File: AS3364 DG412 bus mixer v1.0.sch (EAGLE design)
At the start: 119 parts, among them IC1 PCA9539PW, IC10 DG412-J, IC11 DG412-J, IC14 TL074JT, IC2 TL074JT, IC3 TL072JT, IC4 TL074JT, IC6 TL072JT, IC8 DG412-J, IC9 DG412-J

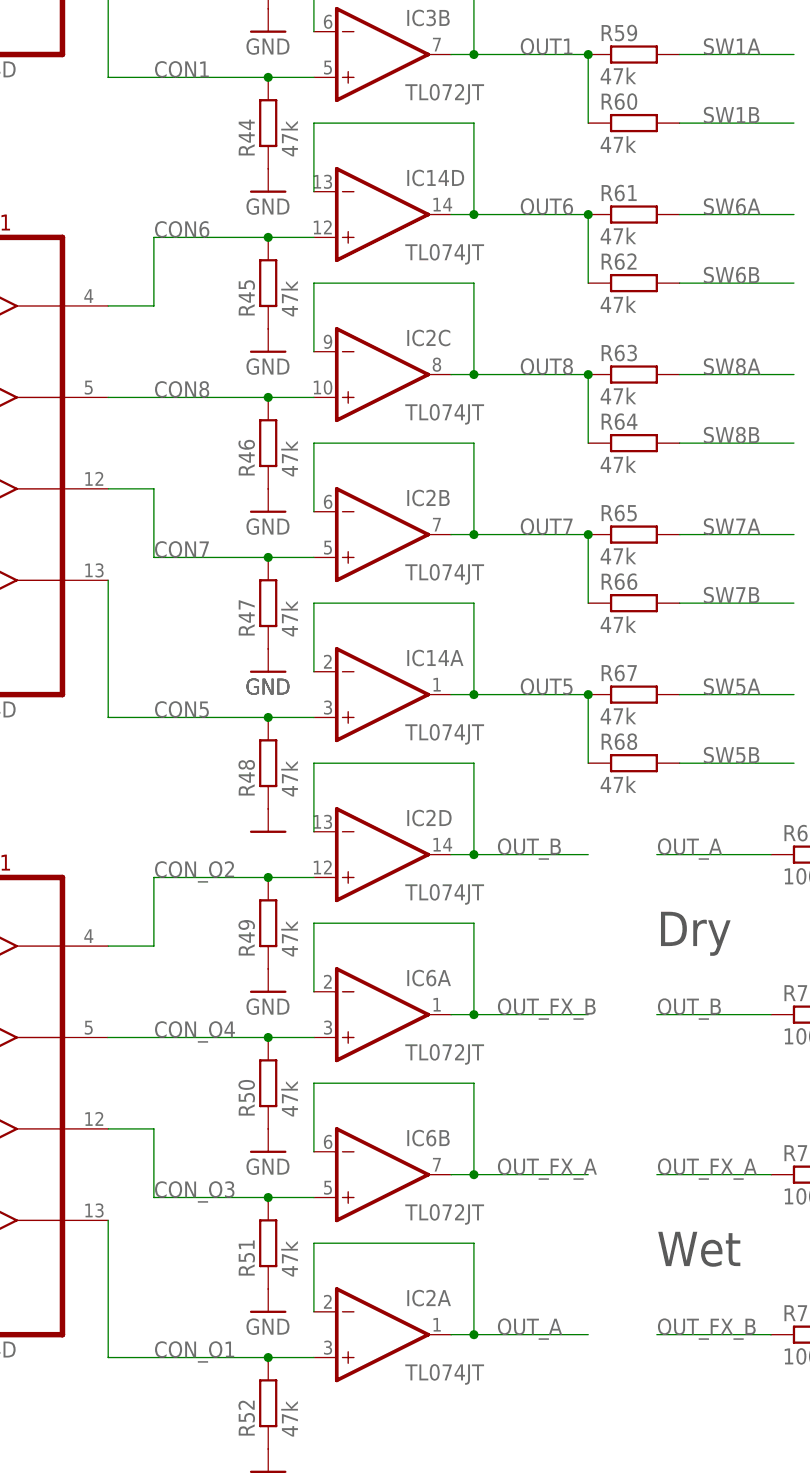
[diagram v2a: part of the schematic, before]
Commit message: Moved dry/wet bus mixer to center to shorten vca-switch distances
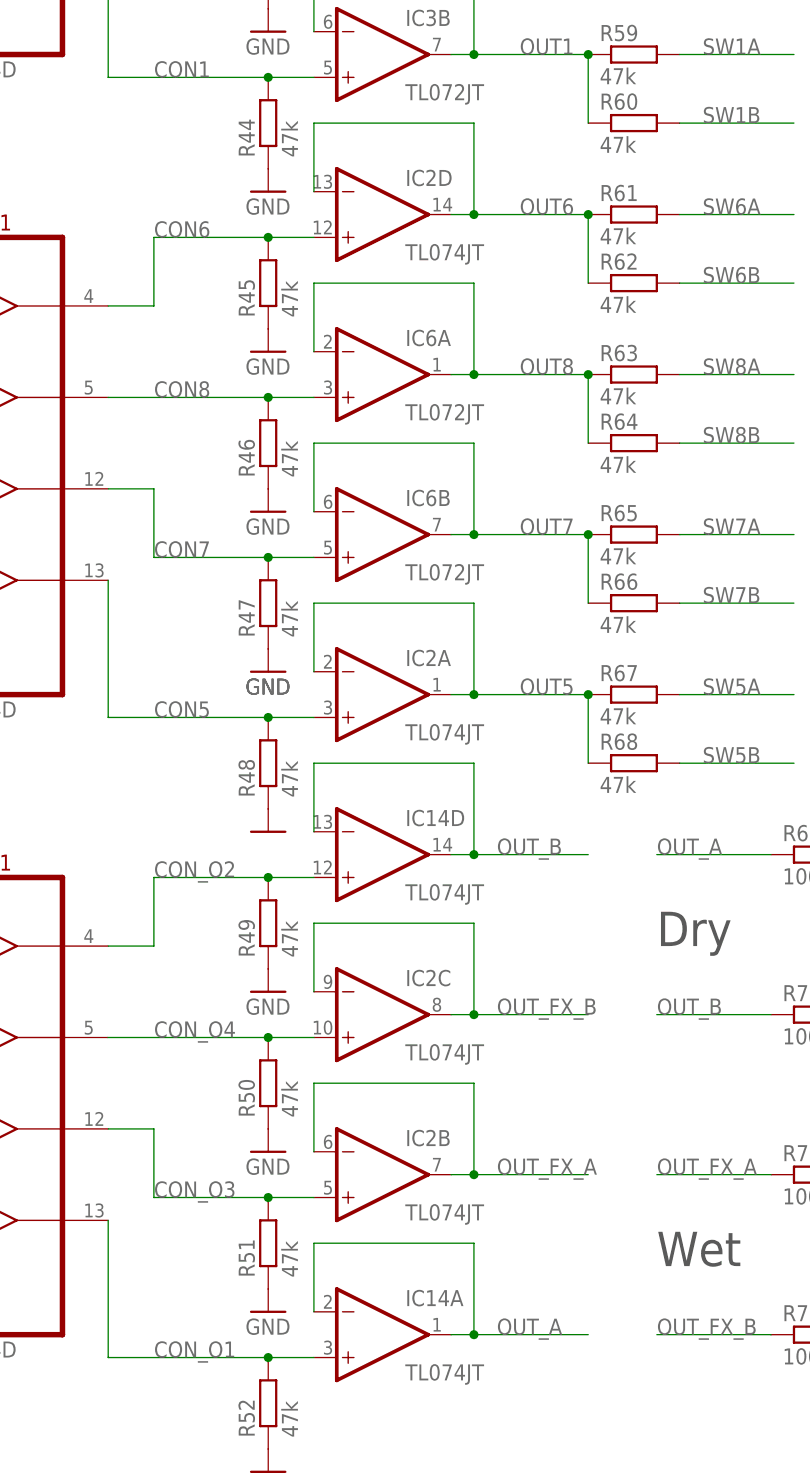
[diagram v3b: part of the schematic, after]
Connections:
- net CON5: now also IC2A.+IN; no longer IC14A.+IN
- net CON6: now also IC2D.+IN; no longer IC14D.+IN
- net CON7: now also IC6B.+IN; no longer IC2B.+IN
- net CON8: now also IC6A.+IN; no longer IC2C.+IN
- net CON_O1: now also IC14A.+IN; no longer IC2A.+IN
- net CON_O2: now also IC14D.+IN; no longer IC2D.+IN
- net CON_O3: now also IC2B.+IN; no longer IC6B.+IN
- net CON_O4: now also IC2C.+IN; no longer IC6A.+IN
- net OUT5: now also IC2A.-IN, IC2A.OUT; no longer IC14A.-IN, IC14A.OUT
- net OUT6: now also IC2D.-IN, IC2D.OUT; no longer IC14D.-IN, IC14D.OUT
- net OUT7: now also IC6B.-IN, IC6B.OUT; no longer IC2B.-IN, IC2B.OUT
- net OUT8: now also IC6A.-IN, IC6A.OUT; no longer IC2C.-IN, IC2C.OUT
- net OUT_A: now also IC14A.-IN, IC14A.OUT; no longer IC2A.-IN, IC2A.OUT
- net OUT_B: now also IC14D.-IN, IC14D.OUT; no longer IC2D.-IN, IC2D.OUT
- net OUT_FX_A: now also IC2B.-IN, IC2B.OUT; no longer IC6B.-IN, IC6B.OUT
- net OUT_FX_B: now also IC2C.-IN, IC2C.OUT; no longer IC6A.-IN, IC6A.OUT
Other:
- moved on the sheet: IC14A, IC14D, IC2A, IC2B, IC2C, IC2D, IC6A, IC6B
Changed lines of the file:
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@@
 <attribute name="VALUE" x="-27.94" y="-71.12" size="1.778" layer="96"/>
-</instance>
-<instance part="IC6" gate="B" x="73.66" y="-93.98" smashed="yes">
-<attribute name="NAME" x="76.2" y="-90.805" size="1.778" layer="95"/>
-<attribute name="VALUE" x="76.2" y="-99.06" size="1.778" layer="96"/>
-</instance>
-<instance part="IC6" gate="A" x="73.66" y="-76.2" smashed="yes">
-<attribute name="NAME" x="76.2" y="-73.025" size="1.778" layer="95"/>
-<attribute name="VALUE" x="76.2" y="-81.28" size="1.778" layer="96"/>
 </instance>
 <instance part="C15" gate="G$1" x="-7.62" y="-109.22" smashed="yes" rot="R90">
@@
 </instance>
 <instance part="IC4" gate="P" x="149.86" y="-167.64" smashed="yes"/>
-<instance part="IC14" gate="A" x="73.66" y="-40.64" smashed="yes">
-<attribute name="NAME" x="76.2" y="-37.465" size="1.778" layer="95"/>
-<attribute name="VALUE" x="76.2" y="-45.72" size="1.778" layer="96"/>
-</instance>
 <instance part="IC14" gate="C" x="73.66" y="66.04" smashed="yes">
 <attribute name="NAME" x="76.2" y="69.215" size="1.778" layer="95"/>
@@
 <attribute name="VALUE" x="76.2" y="43.18" size="1.778" layer="96"/>
 </instance>
-<instance part="IC14" gate="D" x="73.66" y="12.7" smashed="yes">
-<attribute name="NAME" x="76.2" y="15.875" size="1.778" layer="95"/>
-<attribute name="VALUE" x="76.2" y="7.62" size="1.778" layer="96"/>
-</instance>
-<instance part="IC2" gate="C" x="73.66" y="-5.08" smashed="yes">
-<attribute name="NAME" x="76.2" y="-1.905" size="1.778" layer="95"/>
-<attribute name="VALUE" x="76.2" y="-10.16" size="1.778" layer="96"/>
-</instance>
-<instance part="IC2" gate="A" x="73.66" y="-111.76" smashed="yes">
-<attribute name="NAME" x="76.2" y="-108.585" size="1.778" layer="95"/>
-<attribute name="VALUE" x="76.2" y="-116.84" size="1.778" layer="96"/>
-</instance>
-<instance part="IC2" gate="B" x="73.66" y="-22.86" smashed="yes">
-<attribute name="NAME" x="76.2" y="-19.685" size="1.778" layer="95"/>
-<attribute name="VALUE" x="76.2" y="-27.94" size="1.778" layer="96"/>
-</instance>
-<instance part="IC2" gate="D" x="73.66" y="-58.42" smashed="yes">
-<attribute name="NAME" x="76.2" y="-55.245" size="1.778" layer="95"/>
-<attribute name="VALUE" x="76.2" y="-63.5" size="1.778" layer="96"/>
-</instance>
 <instance part="C23" gate="G$1" x="-182.88" y="-33.02" smashed="yes" rot="R180">
 <attribute name="NAME" x="-186.944" y="-28.321" size="1.778" layer="95" rot="R180"/>
 <attribute name="VALUE" x="-186.944" y="-30.861" size="1.778" layer="96" rot="R180"/>
+</instance>
+<instance part="IC2" gate="D" x="73.66" y="12.7" smashed="yes">
+<attribute name="NAME" x="76.2" y="15.875" size="1.778" layer="95"/>
+<attribute name="VALUE" x="76.2" y="7.62" size="1.778" layer="96"/>
+</instance>
+<instance part="IC14" gate="D" x="73.66" y="-58.42" smashed="yes">
+<attribute name="NAME" x="76.2" y="-55.245" size="1.778" layer="95"/>
+<attribute name="VALUE" x="76.2" y="-63.5" size="1.778" layer="96"/>
+</instance>
+<instance part="IC2" gate="A" x="73.66" y="-40.64" smashed="yes">
+<attribute name="NAME" x="76.2" y="-37.465" size="1.778" layer="95"/>
+<attribute name="VALUE" x="76.2" y="-45.72" size="1.778" layer="96"/>
+</instance>
+<instance part="IC14" gate="A" x="73.66" y="-111.76" smashed="yes">
+<attribute name="NAME" x="76.2" y="-108.585" size="1.778" layer="95"/>
+<attribute name="VALUE" x="76.2" y="-116.84" size="1.778" layer="96"/>
+</instance>
+<instance part="IC2" gate="C" x="73.66" y="-76.2" smashed="yes">
+<attribute name="NAME" x="76.2" y="-73.025" size="1.778" layer="95"/>
+<attribute name="VALUE" x="76.2" y="-81.28" size="1.778" layer="96"/>
+</instance>
+<instance part="IC6" gate="A" x="73.66" y="-5.08" smashed="yes">
+<attribute name="NAME" x="76.2" y="-1.905" size="1.778" layer="95"/>
+<attribute name="VALUE" x="76.2" y="-10.16" size="1.778" layer="96"/>
+</instance>
+<instance part="IC2" gate="B" x="73.66" y="-93.98" smashed="yes">
+<attribute name="NAME" x="76.2" y="-90.805" size="1.778" layer="95"/>
+<attribute name="VALUE" x="76.2" y="-99.06" size="1.778" layer="96"/>
+</instance>
+<instance part="IC6" gate="B" x="73.66" y="-22.86" smashed="yes">
+<attribute name="NAME" x="76.2" y="-19.685" size="1.778" layer="95"/>
+<attribute name="VALUE" x="76.2" y="-27.94" size="1.778" layer="96"/>
 </instance>
 </instances>
@@
 <wire x1="66.04" y1="10.16" x2="60.96" y2="10.16" width="0.1524" layer="91"/>
 <junction x="60.96" y="10.16"/>
-<pinref part="IC14" gate="D" pin="+IN"/>
+<pinref part="IC2" gate="D" pin="+IN"/>
 </segment>
 </net>
@@
 <wire x1="66.04" y1="-7.62" x2="60.96" y2="-7.62" width="0.1524" layer="91"/>
 <junction x="60.96" y="-7.62"/>
-<pinref part="IC2" gate="C" pin="+IN"/>
+<pinref part="IC6" gate="A" pin="+IN"/>
 </segment>
 </net>
@@
 <wire x1="66.04" y1="-25.4" x2="60.96" y2="-25.4" width="0.1524" layer="91"/>
 <junction x="60.96" y="-25.4"/>
-<pinref part="IC2" gate="B" pin="+IN"/>
+<pinref part="IC6" gate="B" pin="+IN"/>
 </segment>
 </net>
@@
 <wire x1="66.04" y1="-43.18" x2="60.96" y2="-43.18" width="0.1524" layer="91"/>
 <junction x="60.96" y="-43.18"/>
-<pinref part="IC14" gate="A" pin="+IN"/>
+<pinref part="IC2" gate="A" pin="+IN"/>
 </segment>
 </net>
@@
 <wire x1="96.52" y1="-22.86" x2="96.52" y2="-30.48" width="0.1524" layer="91"/>
 <junction x="96.52" y="-22.86"/>
-<pinref part="IC2" gate="B" pin="-IN"/>
-<pinref part="IC2" gate="B" pin="OUT"/>
+<pinref part="IC6" gate="B" pin="-IN"/>
+<pinref part="IC6" gate="B" pin="OUT"/>
 </segment>
 </net>
@@
 <wire x1="96.52" y1="-5.08" x2="96.52" y2="-12.7" width="0.1524" layer="91"/>
 <junction x="96.52" y="-5.08"/>
-<pinref part="IC2" gate="C" pin="-IN"/>
-<pinref part="IC2" gate="C" pin="OUT"/>
+<pinref part="IC6" gate="A" pin="-IN"/>
+<pinref part="IC6" gate="A" pin="OUT"/>
 </segment>
 </net>
@@
 <wire x1="96.52" y1="-40.64" x2="96.52" y2="-48.26" width="0.1524" layer="91"/>
 <junction x="96.52" y="-40.64"/>
-<pinref part="IC14" gate="A" pin="-IN"/>
-<pinref part="IC14" gate="A" pin="OUT"/>
+<pinref part="IC2" gate="A" pin="-IN"/>
+<pinref part="IC2" gate="A" pin="OUT"/>
 </segment>
 </net>
@@
 <wire x1="96.52" y1="12.7" x2="96.52" y2="5.08" width="0.1524" layer="91"/>
 <junction x="96.52" y="12.7"/>
-<pinref part="IC14" gate="D" pin="-IN"/>
-<pinref part="IC14" gate="D" pin="OUT"/>
+<pinref part="IC2" gate="D" pin="-IN"/>
+<pinref part="IC2" gate="D" pin="OUT"/>
 </segment>
 </net>
@@
 <wire x1="66.04" y1="-60.96" x2="60.96" y2="-60.96" width="0.1524" layer="91"/>
 <junction x="60.96" y="-60.96"/>
-<pinref part="IC2" gate="D" pin="+IN"/>
+<pinref part="IC14" gate="D" pin="+IN"/>
 </segment>
 </net>
@@
 <label x="48.26" y="-78.74" size="1.778" layer="95"/>
 <pinref part="R50" gate="G$1" pin="2"/>
-<pinref part="IC6" gate="A" pin="+IN"/>
 <wire x1="60.96" y1="-78.74" x2="66.04" y2="-78.74" width="0.1524" layer="91"/>
 <junction x="60.96" y="-78.74"/>
+<pinref part="IC2" gate="C" pin="+IN"/>
 </segment>
 </net>
@@
 <pinref part="R51" gate="G$1" pin="2"/>
 <wire x1="48.26" y1="-96.52" x2="60.96" y2="-96.52" width="0.1524" layer="91"/>
-<pinref part="IC6" gate="B" pin="+IN"/>
 <wire x1="66.04" y1="-96.52" x2="60.96" y2="-96.52" width="0.1524" layer="91"/>
 <junction x="60.96" y="-96.52"/>
+<pinref part="IC2" gate="B" pin="+IN"/>
 </segment>
 </net>
@@
 <wire x1="66.04" y1="-114.3" x2="60.96" y2="-114.3" width="0.1524" layer="91"/>
 <junction x="60.96" y="-114.3"/>
-<pinref part="IC2" gate="A" pin="+IN"/>
+<pinref part="IC14" gate="A" pin="+IN"/>
 </segment>
 </net>
@@
 <wire x1="83.82" y1="-76.2" x2="96.52" y2="-76.2" width="0.1524" layer="91"/>
 <junction x="83.82" y="-76.2"/>
-<pinref part="IC6" gate="A" pin="OUT"/>
 <wire x1="66.04" y1="-73.66" x2="66.04" y2="-66.04" width="0.1524" layer="91"/>
-<pinref part="IC6" gate="A" pin="-IN"/>
 <wire x1="66.04" y1="-66.04" x2="83.82" y2="-66.04" width="0.1524" layer="91"/>
 <label x="86.36" y="-76.2" size="1.778" layer="95"/>
+<pinref part="IC2" gate="C" pin="-IN"/>
+<pinref part="IC2" gate="C" pin="OUT"/>
 </segment>
 <segment>
@@
 <wire x1="83.82" y1="-93.98" x2="96.52" y2="-93.98" width="0.1524" layer="91"/>
 <junction x="83.82" y="-93.98"/>
-<pinref part="IC6" gate="B" pin="OUT"/>
 <wire x1="66.04" y1="-91.44" x2="66.04" y2="-83.82" width="0.1524" layer="91"/>
-<pinref part="IC6" gate="B" pin="-IN"/>
 <wire x1="83.82" y1="-83.82" x2="66.04" y2="-83.82" width="0.1524" layer="91"/>
 <label x="86.36" y="-93.98" size="1.778" layer="95"/>
+<pinref part="IC2" gate="B" pin="-IN"/>
+<pinref part="IC2" gate="B" pin="OUT"/>
 </segment>
 <segment>
@@
 <wire x1="66.04" y1="-101.6" x2="83.82" y2="-101.6" width="0.1524" layer="91"/>
 <label x="86.36" y="-111.76" size="1.778" layer="95"/>
-<pinref part="IC2" gate="A" pin="-IN"/>
-<pinref part="IC2" gate="A" pin="OUT"/>
+<pinref part="IC14" gate="A" pin="-IN"/>
+<pinref part="IC14" gate="A" pin="OUT"/>
 </segment>
 <segment>
@@
 <wire x1="66.04" y1="-48.26" x2="83.82" y2="-48.26" width="0.1524" layer="91"/>
 <label x="86.36" y="-58.42" size="1.778" layer="95"/>
-<pinref part="IC2" gate="D" pin="-IN"/>
-<pinref part="IC2" gate="D" pin="OUT"/>
-</segment>
-<segment>
+<pinref part="IC14" gate="D" pin="-IN"/>
+<pinref part="IC14" gate="D" pin="OUT"/>
+</segment>
+<segment>

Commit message: Almost all signals routed except outputs
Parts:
- removed SV1: (no value), joakim:MA16-2WJ
- added SV10, SV11, SV12, SV13, SV14, SV15, SV16, SV17, SV18, SV19, SV2, SV20, SV21, SV22, SV23, SV24, SV25, SV26, SV27, SV28, SV29, SV3, SV30, SV31, SV4, SV5, SV6, SV7, SV8, SV9: (no value), joakim:MA01-1JP
- R69, R70, R71, R72: device rcl:R-EU_R0603 -> rcl:R-EU_R0402
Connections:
- new net RST: SV6.1
- net +12V: now also SV21.1; no longer SV1.18
- net +3V3: now also SV2.1; no longer SV1.31
- net -12V: now also SV31.1; no longer SV1.15
- net CV1: now also SV11.1; no longer SV1.26
- net CV2: now also SV12.1; no longer SV1.24
- net CV3: now also SV13.1; no longer SV1.22
- net CV4: now also SV14.1; no longer SV1.20
- net CV5: now also SV27.1; no longer SV1.12
- net CV6: now also SV28.1; no longer SV1.10
- net CV7: now also SV29.1; no longer SV1.8
- net CV8: now also SV30.1; no longer SV1.6
- net CV_A_DRY: now also SV15.1
- net CV_A_WET: now also SV16.1
- net CV_B_DRY: now also SV17.1
- net CV_B_WET: now also SV18.1
- net DGND: now also SV5.1; no longer SV1.29
- net GND: now also SV22.1; no longer SV1.17
- net IN1: now also SV7.1; no longer SV1.25
- net IN2: now also SV8.1; no longer SV1.23
- net IN3: now also SV9.1; no longer SV1.21
- net IN4: now also SV10.1; no longer SV1.19
- net IN5: now also SV23.1; no longer SV1.11
- net IN6: now also SV24.1; no longer SV1.9
- net IN7: now also SV25.1; no longer SV1.7
- net IN8: now also SV26.1; no longer SV1.5
- net LPF_IN_100K_MIX: now also SV20.1
- net SCL: now also SV4.1; no longer SV1.32
- net SDA: now also SV3.1; no longer SV1.30
- net SVF_IN_100K_MIX: now also SV19.1
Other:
- moved on the sheet: C23, IC1, R1

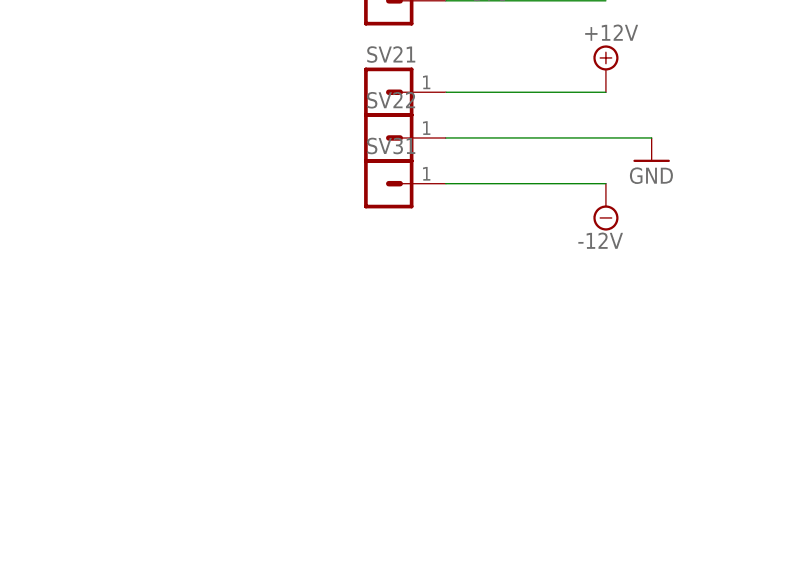
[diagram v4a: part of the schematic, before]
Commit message: Mostly traced, need to do ground and cleanup
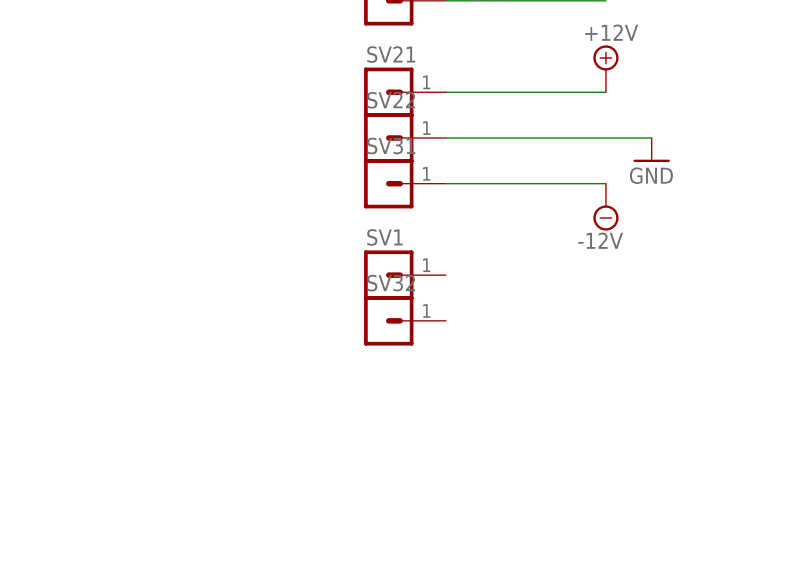
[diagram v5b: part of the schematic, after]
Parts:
- added SV1, SV32: (no value), joakim:MA01-1JP
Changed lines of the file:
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@@
 <part name="SUPPLY3" library="supply2" library_urn="urn:adsk.eagle:library:372" deviceset="+12V" device=""/>
 <part name="SUPPLY4" library="supply2" library_urn="urn:adsk.eagle:library:372" deviceset="-12V" device=""/>
+<part name="SV1" library="joakim" deviceset="MA01-1J" device="P"/>
+<part name="SV32" library="joakim" deviceset="MA01-1J" device="P"/>
 </parts>
 <sheets>
@@
 <attribute name="VALUE" x="-79.375" y="-83.439" size="1.778" layer="96"/>
 </instance>
+<instance part="SV1" gate="G$1" x="-101.6" y="-86.36" smashed="yes">
+<attribute name="VALUE" x="-102.87" y="-91.44" size="1.778" layer="96"/>
+<attribute name="NAME" x="-102.87" y="-83.058" size="1.778" layer="95"/>
+</instance>
+<instance part="SV32" gate="G$1" x="-101.6" y="-91.44" smashed="yes">
+<attribute name="VALUE" x="-102.87" y="-96.52" size="1.778" layer="96"/>
+<attribute name="NAME" x="-102.87" y="-88.138" size="1.778" layer="95"/>
+</instance>
 </instances>

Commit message: Finished tracing, need part numbers
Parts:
- R1: value 1K -> 10k; device rcl:R-EU_R0603 -> rcl:R-EU_R0402
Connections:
- net N$4 renamed VL
- removed net N$81: IC1.!RESET, R1.2
- removed net RST: SV6.1
- new net !RST: IC1.!RESET, R1.2, SV6.1
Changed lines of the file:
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@@
 <part name="+3V17" library="supply1" library_urn="urn:adsk.eagle:library:371" deviceset="+3V3" device=""/>
 <part name="SUPPLY30" library="supply2" library_urn="urn:adsk.eagle:library:372" deviceset="DGND" device=""/>
-<part name="R1" library="rcl" library_urn="urn:adsk.eagle:library:334" deviceset="R-EU_" device="R0603" package3d_urn="urn:adsk.eagle:package:23555/3" value="1K"/>
+<part name="R1" library="rcl" library_urn="urn:adsk.eagle:library:334" deviceset="R-EU_" device="R0402" package3d_urn="urn:adsk.eagle:package:23547/3" value="10k"/>
 <part name="+3V21" library="supply1" library_urn="urn:adsk.eagle:library:371" deviceset="+3V3" device=""/>
 <part name="C10" library="rcl" library_urn="urn:adsk.eagle:library:334" deviceset="C-EU" device="C0402" package3d_urn="urn:adsk.eagle:package:23626/2" value="100nF"/>
@@
 </segment>
 </net>
-<net name="N$81" class="0">
-<segment>
-<pinref part="IC1" gate="G$1" pin="!RESET"/>
-<pinref part="R1" gate="G$1" pin="2"/>
-</segment>
-</net>
-<net name="N$4" class="0">
+<net name="VL" class="0">
 <segment>
 <pinref part="IC8" gate="_WL" pin="VL"/>
@@
 <wire x1="246.38" y1="66.04" x2="246.38" y2="63.5" width="0.1524" layer="91"/>
 <junction x="254" y="66.04"/>
+<label x="248.92" y="66.04" size="1.778" layer="95"/>
 </segment>
 </net>
@@
 </segment>
 </net>
-<net name="RST" class="0">
+<net name="!RST" class="0">
 <segment>
 <pinref part="SV6" gate="G$1" pin="1"/>
@@
 <label x="-91.44" y="96.52" size="1.778" layer="95"/>
 </segment>
+<segment>
+<pinref part="IC1" gate="G$1" pin="!RESET"/>
+<pinref part="R1" gate="G$1" pin="2"/>
+<wire x1="198.12" y1="-147.32" x2="198.12" y2="-152.4" width="0.1524" layer="91"/>
+<junction x="198.12" y="-147.32"/>
+<wire x1="198.12" y1="-152.4" x2="177.8" y2="-152.4" width="0.1524" layer="91"/>
+<label x="177.8" y="-152.4" size="1.778" layer="95"/>
+</segment>
 </net>

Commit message: Only need to fix text
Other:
- note removed: "TODO: Make panner from single CV`?"
